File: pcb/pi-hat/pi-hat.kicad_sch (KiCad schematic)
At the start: 15 parts, among them IC3 THVD1420DR, J1 GPIO, J2 5555140-2, U1 CAT24C256

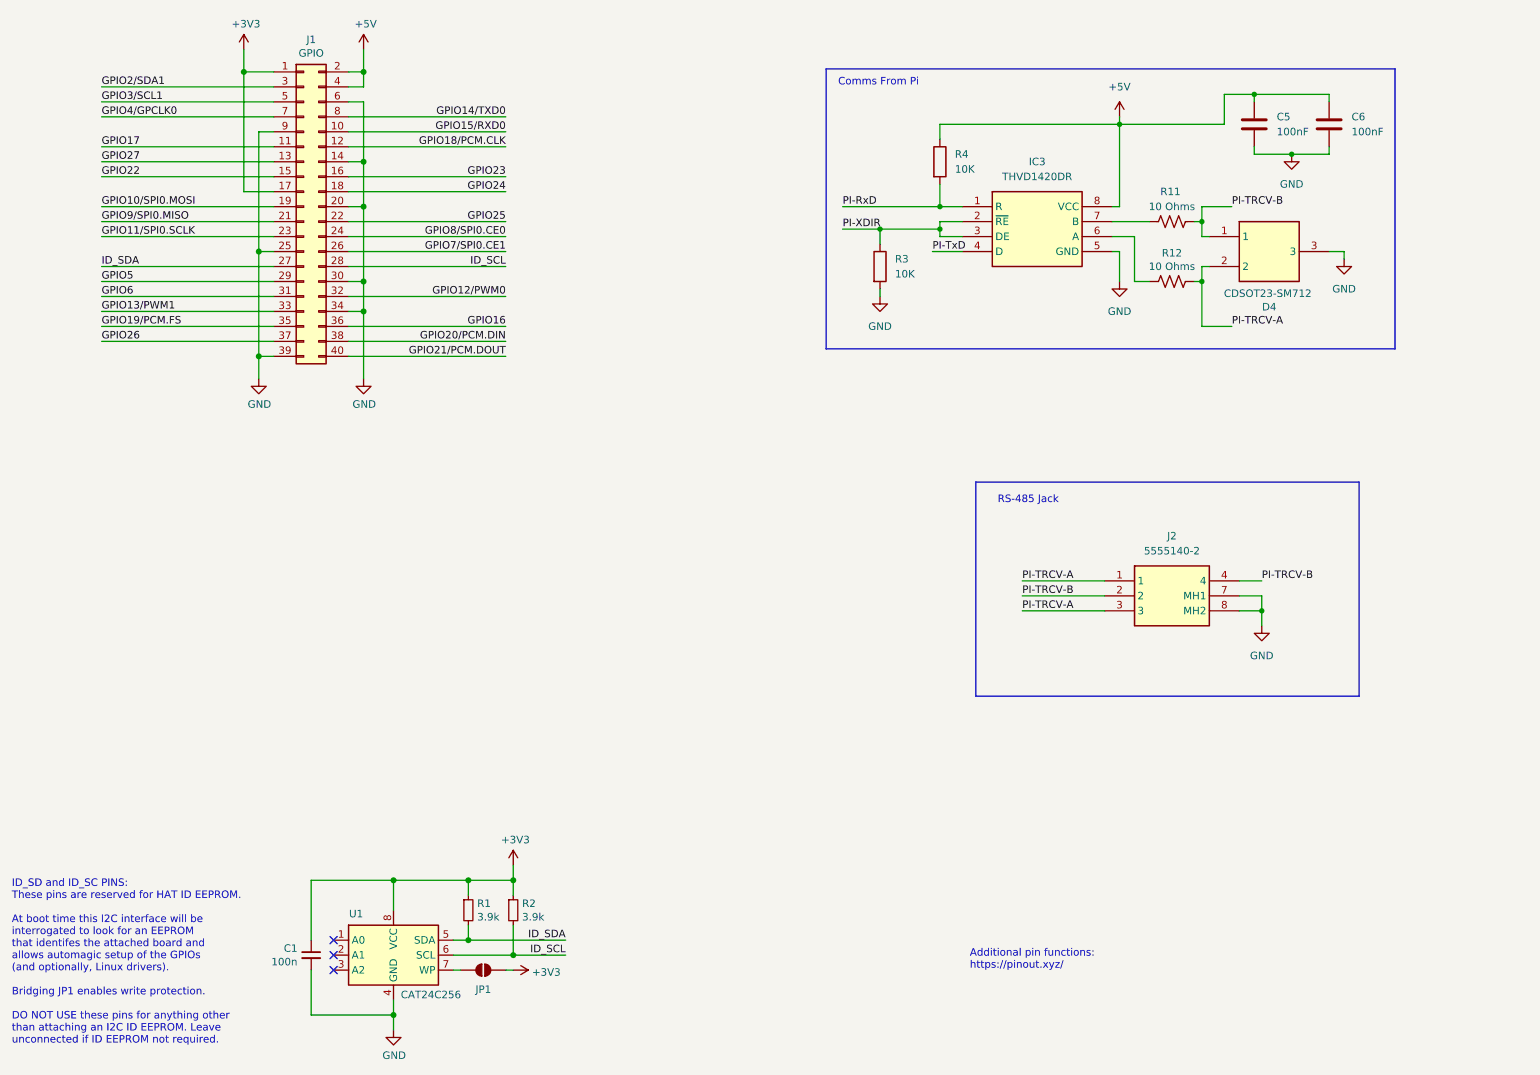
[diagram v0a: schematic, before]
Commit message: pcb: 3.3V transceiver supply, second Row Bus chain, fab outputs
The THVD1420DR transceivers ran at VCC=5V while driving 3.3V-only GPIOs on
both boards. Per the datasheet the receiver output swings to VCC-0.4V min
(~4.6-4.8V at 5V), and the RX pull-ups went to 5V as well, so both the Pi's
and the RP2350's inputs sat out of spec. Both boards were bodged to 3.3V on
the bench; these schematics bring the sources in line.

pi-hat:
- IC3 supply, decoupling and RX pull-up moved from +5V to +3V3; no +5V net
  remains on the board.
- Second Row Bus chain added (IC4) so the 8 rows split across two chains -
  see docs/row-bus-protocol.md for why one chain no longer fits the frame
  budget. Chain A on uart0 (GPIO14/15), chain B on uart2 (GPIO4/5).
- Both direction lines moved onto the UARTs' own RTS pins, GPIO17 and
  GPIO7, so the kernel's RS-485 mode can eventually drive them with
  hardware timing instead of the host's busy-wait.
- Single RJ45 carries both chains on correctly-paired T568B conductors:
  chain A on pins 1-2, chain B on 3-6, grounds on the blue and brown pairs.

row-controller:
- Both transceivers, the INA220 and its I2C pull-ups moved to +3V3. +5V now
  only feeds the Xiao's VUSB input and the regulator that makes it.
- INA220 VBUS now senses +12V through the 5 mOhm shunt, matching what
  docs/row-bus-protocol.md's POWER command has always claimed it measures;
  it previously sat on the 5V rail and reported ~4.8V.

Also adds v1.0/1.2 gerbers and BOM CSVs, following the existing
gerber-1.1 pattern.

Reviewed the pi-hat netlist in detail - header pins, transceiver
orientation, rails, termination and pairing all check out. The
row-controller and tile changes are carried as-is.

Co-Authored-By: Claude Opus 5 <noreply@anthropic.com>
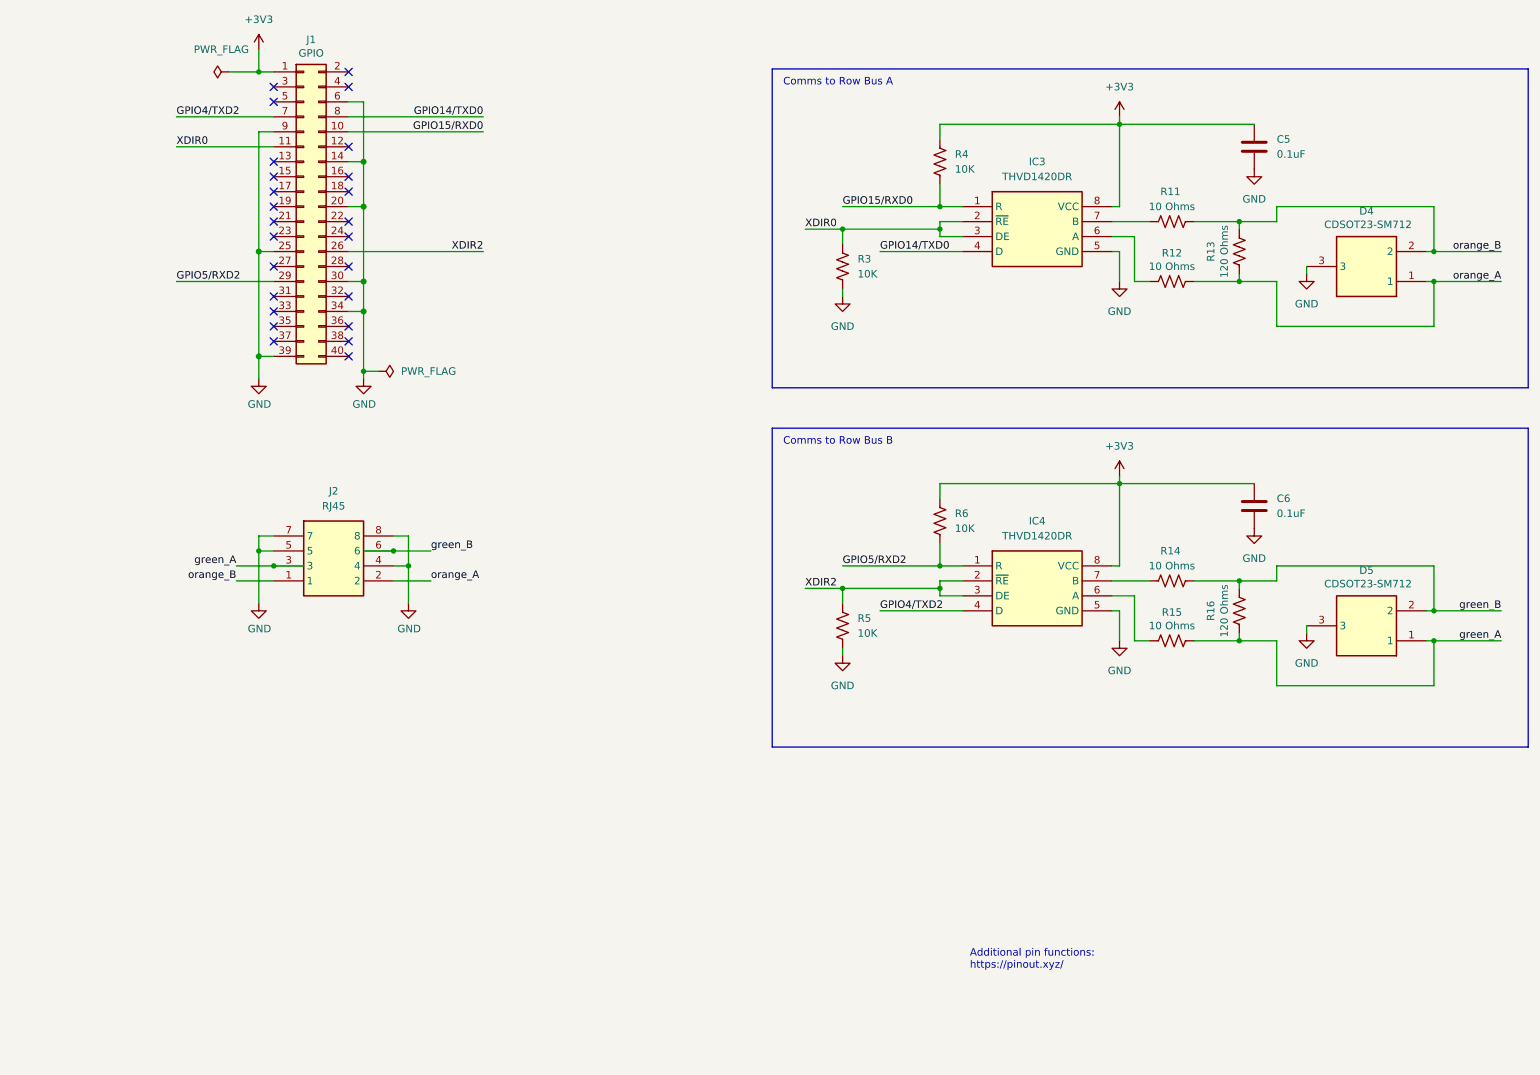
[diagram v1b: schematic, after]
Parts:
- removed C1: 100n, symbol Device:C_Small
- removed J2: 5555140-2, 5555140-2:55551402, symbol 5555140-2:5555140-2
- removed JP1: ID_WP, symbol Jumper:SolderJumper_2_Open
- removed R1, R2: 3.9k, symbol Device:R_Small
- removed U1: CAT24C256, symbol Memory_EEPROM:CAT24C256
- added D5: CDSOT23-SM712, Garth:SOT95P230X117-3N, symbol Garth Libraries:CDSOT23-SM712
- added IC4: THVD1420DR, THVD1420DR:SOIC127P600X175-8N, symbol THVD1420DR:THVD1420DR
- added J2: RJ45, Garth:MJ3225880, symbol Garth Libraries:MJ3225-88-0
- added R13, R16: 120 Ohms, Resistor_SMD:R_0805_2012Metric_Pad1.20x1.40mm_HandSolder, symbol Device:R_US
- added R14, R15: 10 Ohms, Resistor_SMD:R_1206_3216Metric_Pad1.30x1.75mm_HandSolder, symbol Device:R_US
- added R5, R6: 10K, Resistor_SMD:R_0805_2012Metric_Pad1.20x1.40mm_HandSolder, symbol Device:R_US
- C5, C6: value 100nF -> 0.1uF
- R3, R4: symbol Device:R -> Device:R_US
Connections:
- net PI-RxD is gone; now on net GPIO15/RXD0: IC3.1 (R), R4.2
- net PI-TxD is gone; now on net GPIO14/TXD0: IC3.4 (D)
- net PI-XDIR is gone; now on net XDIR0: IC3.2 (~{RE}), IC3.3 (DE), R3.1
- net +3V3: now also C5.1, C6.1, IC3.8 (VCC), R4.1, IC4.8 (VCC), R6.1; no longer J1.17 (Pin_17)
- net GND: now also D5.3, IC4.5 (GND), J2.4, J2.5, J2.7, J2.8, R5.2
- removed net +5V: C5.1, C6.1, IC3.8 (VCC), J1.2 (Pin_2), J1.4 (Pin_4), R4.1
- net GPIO10/SPI0.MOSI: no longer names the net of J1.19 (Pin_19)
- net GPIO11/SPI0.SCLK: no longer names the net of J1.23 (Pin_23)
- net GPIO12/PWM0: no longer names the net of J1.32 (Pin_32)
- net GPIO13/PWM1: no longer names the net of J1.33 (Pin_33)
- net GPIO16: no longer names the net of J1.36 (Pin_36)
- net GPIO17 renamed XDIR0
- net GPIO18/PCM.CLK: no longer names the net of J1.12 (Pin_12)
- net GPIO19/PCM.FS: no longer names the net of J1.35 (Pin_35)
- net GPIO20/PCM.DIN: no longer names the net of J1.38 (Pin_38)
- net GPIO21/PCM.DOUT: no longer names the net of J1.40 (Pin_40)
- net GPIO22: no longer names the net of J1.15 (Pin_15)
- net GPIO23: no longer names the net of J1.16 (Pin_16)
- net GPIO24: no longer names the net of J1.18 (Pin_18)
- net GPIO25: no longer names the net of J1.22 (Pin_22)
- net GPIO26: no longer names the net of J1.37 (Pin_37)
- net GPIO27: no longer names the net of J1.13 (Pin_13)
- net GPIO2/SDA1: no longer names the net of J1.3 (Pin_3)
- net GPIO3/SCL1: no longer names the net of J1.5 (Pin_5)
- net GPIO4/GPCLK0 renamed GPIO4/TXD2
- net GPIO4/TXD2: now also IC4.4 (D)
- net GPIO5 renamed GPIO5/RXD2
- net GPIO5/RXD2: now also IC4.1 (R), R6.2
- net GPIO6: no longer names the net of J1.31 (Pin_31)
- net GPIO7/SPI0.CE1 renamed XDIR2
- net XDIR2: now also IC4.2 (~{RE}), IC4.3 (DE), R5.1
- net GPIO8/SPI0.CE0: no longer names the net of J1.24 (Pin_24)
- net GPIO9/SPI0.MISO: no longer names the net of J1.21 (Pin_21)
- net ID_SCL: no longer names the net of J1.28 (Pin_28)
- net ID_SDA: no longer names the net of J1.27 (Pin_27)
- net PI-TRCV-A renamed orange_A
- net orange_A: now also D4.1, J2.2, R13.1; no longer D4.2
- net PI-TRCV-B renamed orange_B
- net orange_B: now also D4.2, J2.1, R13.2; no longer D4.1
- new net: IC4.6 (A), R15.1
- new net: IC4.7 (B), R14.1
- new net green_A: D5.1, J2.3, R15.2, R16.1
- new net green_B: D5.2, J2.6, R14.2, R16.2
- no-connect marks 3 -> 25
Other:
- note added: "Comms to Row Bus A"
- note added: "Comms to Row Bus B"
- note removed: "Comms From Pi"
- note removed: "ID_SD and ID_SC PINS: These pins are reserved for HAT ID EEPROM. At boot time this I2C interface will be interrogated to look for an EEPROM that identifes the attached board and allows automagic setup of the GPIOs (and optionally, Linux drivers). Bridging JP1 enables write protection. DO NOT USE these pins for anything other than attaching an I2C ID EEPROM. Leave unconnected if ID EEPROM not requ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"
- note removed: "RS-485 Jack"
- moved on the sheet: C5
